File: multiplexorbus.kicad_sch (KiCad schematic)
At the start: 4 parts, among them J2 Conn_02x06_Odd_Even, J3 Conn_02x06_Odd_Even, J4 Conn_02x17_Odd_Even, J5 Conn_02x17_Odd_Even

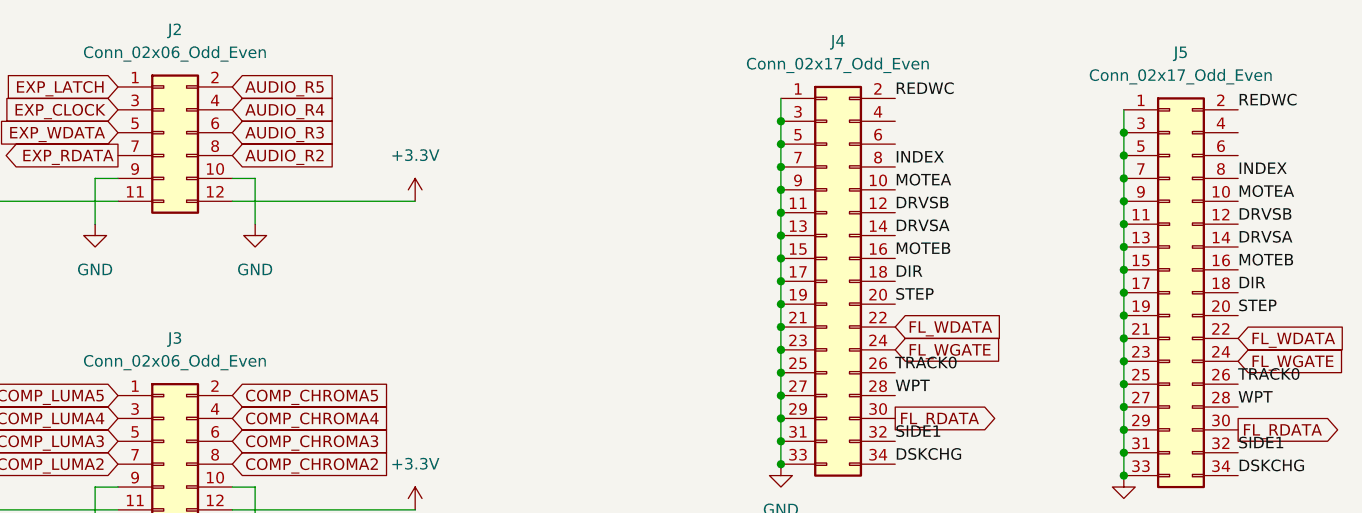
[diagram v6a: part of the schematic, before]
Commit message: work on rerouting board to fit current limiting resistors #1
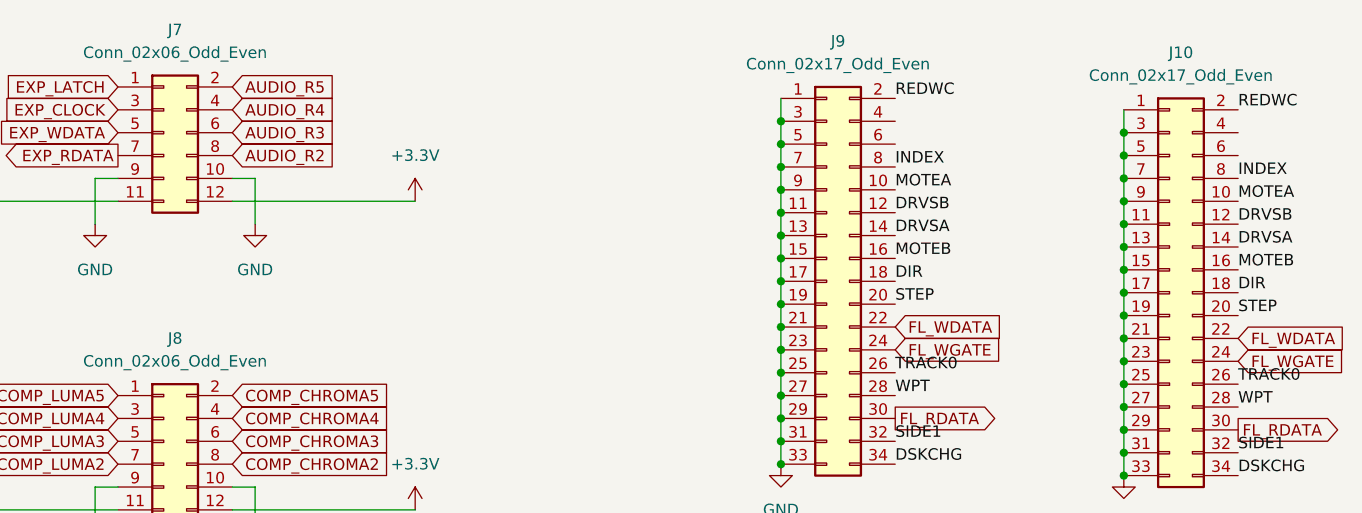
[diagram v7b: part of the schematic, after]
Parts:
- renumbered J5 to J10, J2 to J7, J3 to J8, J4 to J9
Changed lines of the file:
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@@
   (symbol (lib_id "Connector_Generic:Conn_02x06_Odd_Even") (at 77.47 45.72 0) (unit 1)
     (in_bom yes) (on_board yes) (fields_autoplaced)
-    (property "Reference" "J2" (id 0) (at 78.74 34.29 0))
+    (property "Reference" "J7" (id 0) (at 78.74 34.29 0))
     (property "Value" "Conn_02x06_Odd_Even" (id 1) (at 78.74 36.83 0))
     (property "Footprint" "Connector_PinHeader_2.54mm:PinHeader_2x06_P2.54mm_Vertical" (id 2) (at 77.47 45.72 0)
@@
   (symbol (lib_id "Connector_Generic:Conn_02x17_Odd_Even") (at 151.13 62.23 0) (unit 1)
     (in_bom yes) (on_board yes) (fields_autoplaced)
-    (property "Reference" "J4" (id 0) (at 152.4 35.56 0))
+    (property "Reference" "J9" (id 0) (at 152.4 35.56 0))
     (property "Value" "Conn_02x17_Odd_Even" (id 1) (at 152.4 38.1 0))
     (property "Footprint" "Connector_PinHeader_2.54mm:PinHeader_2x17_P2.54mm_Vertical" (id 2) (at 151.13 62.23 0)
@@
   (symbol (lib_id "power:+3.3V") (at 105.41 87.63 0) (unit 1)
     (in_bom yes) (on_board yes) (fields_autoplaced)
-    (property "Reference" "#PWR0147" (id 0) (at 105.41 91.44 0)
+    (property "Reference" "#PWR077" (id 0) (at 105.41 91.44 0)
       (effects (font (size 1.27 1.27)) hide)
     )
@@
   (symbol (lib_id "power:GND") (at 69.85 90.17 0) (unit 1)
     (in_bom yes) (on_board yes) (fields_autoplaced)
-    (property "Reference" "#PWR0148" (id 0) (at 69.85 96.52 0)
+    (property "Reference" "#PWR073" (id 0) (at 69.85 96.52 0)
       (effects (font (size 1.27 1.27)) hide)
     )
@@
   (symbol (lib_id "power:+3.3V") (at 105.41 53.34 0) (unit 1)
     (in_bom yes) (on_board yes) (fields_autoplaced)
-    (property "Reference" "#PWR0146" (id 0) (at 105.41 57.15 0)
+    (property "Reference" "#PWR076" (id 0) (at 105.41 57.15 0)
       (effects (font (size 1.27 1.27)) hide)
     )
@@
   (symbol (lib_id "power:GND") (at 87.63 55.88 0) (unit 1)
     (in_bom yes) (on_board yes) (fields_autoplaced)
-    (property "Reference" "#PWR0145" (id 0) (at 87.63 62.23 0)
+    (property "Reference" "#PWR074" (id 0) (at 87.63 62.23 0)
       (effects (font (size 1.27 1.27)) hide)
     )
@@
   (symbol (lib_id "power:GND") (at 184.15 83.82 0) (unit 1)
     (in_bom yes) (on_board yes) (fields_autoplaced)
-    (property "Reference" "#PWR0150" (id 0) (at 184.15 90.17 0)
+    (property "Reference" "#PWR079" (id 0) (at 184.15 90.17 0)
       (effects (font (size 1.27 1.27)) hide)
     )
@@
   (symbol (lib_id "power:GND") (at 87.63 90.17 0) (unit 1)
     (in_bom yes) (on_board yes) (fields_autoplaced)
-    (property "Reference" "#PWR0149" (id 0) (at 87.63 96.52 0)
+    (property "Reference" "#PWR075" (id 0) (at 87.63 96.52 0)
       (effects (font (size 1.27 1.27)) hide)
     )
@@
   (symbol (lib_id "Connector_Generic:Conn_02x06_Odd_Even") (at 77.47 80.01 0) (unit 1)
     (in_bom yes) (on_board yes) (fields_autoplaced)
-    (property "Reference" "J3" (id 0) (at 78.74 68.58 0))
+    (property "Reference" "J8" (id 0) (at 78.74 68.58 0))
     (property "Value" "Conn_02x06_Odd_Even" (id 1) (at 78.74 71.12 0))
     (property "Footprint" "Connector_PinHeader_2.54mm:PinHeader_2x06_P2.54mm_Vertical" (id 2) (at 77.47 80.01 0)
@@
   (symbol (lib_id "Connector_Generic:Conn_02x17_Odd_Even") (at 189.23 63.5 0) (unit 1)
     (in_bom yes) (on_board yes) (fields_autoplaced)
-    (property "Reference" "J5" (id 0) (at 190.5 36.83 0))
+    (property "Reference" "J10" (id 0) (at 190.5 36.83 0))
     (property "Value" "Conn_02x17_Odd_Even" (id 1) (at 190.5 39.37 0))
     (property "Footprint" "Connector_PinHeader_2.54mm:PinHeader_2x17_P2.54mm_Vertical" (id 2) (at 189.23 63.5 0)
@@
   (symbol (lib_id "power:GND") (at 69.85 55.88 0) (unit 1)
     (in_bom yes) (on_board yes) (fields_autoplaced)
-    (property "Reference" "#PWR0142" (id 0) (at 69.85 62.23 0)
+    (property "Reference" "#PWR072" (id 0) (at 69.85 62.23 0)
       (effects (font (size 1.27 1.27)) hide)
     )
@@
   (symbol (lib_id "power:+3.3V") (at 53.34 53.34 0) (unit 1)
     (in_bom yes) (on_board yes) (fields_autoplaced)
-    (property "Reference" "#PWR0143" (id 0) (at 53.34 57.15 0)
+    (property "Reference" "#PWR070" (id 0) (at 53.34 57.15 0)
       (effects (font (size 1.27 1.27)) hide)
     )
@@
   (symbol (lib_id "power:+3.3V") (at 53.34 87.63 0) (unit 1)
     (in_bom yes) (on_board yes) (fields_autoplaced)
-    (property "Reference" "#PWR0144" (id 0) (at 53.34 91.44 0)
+    (property "Reference" "#PWR071" (id 0) (at 53.34 91.44 0)
       (effects (font (size 1.27 1.27)) hide)
     )
@@
   (symbol (lib_id "power:GND") (at 146.05 82.55 0) (unit 1)
     (in_bom yes) (on_board yes) (fields_autoplaced)
-    (property "Reference" "#PWR0141" (id 0) (at 146.05 88.9 0)
-      (effects (font (size 1.27 1.27)) hide)
-    )
+    (property "Reference" "#PWR078" (id 0) (at 146.05 88.9 0)
+      (effects (font (size 1.27 1.27)) hide)
+    )
